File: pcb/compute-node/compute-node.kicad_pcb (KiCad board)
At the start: 2 copper layers, 30 x 26.8 mm, 6 parts, among them J1 UART, U1 PicoNode-Card, U2 STM32F030F4Px

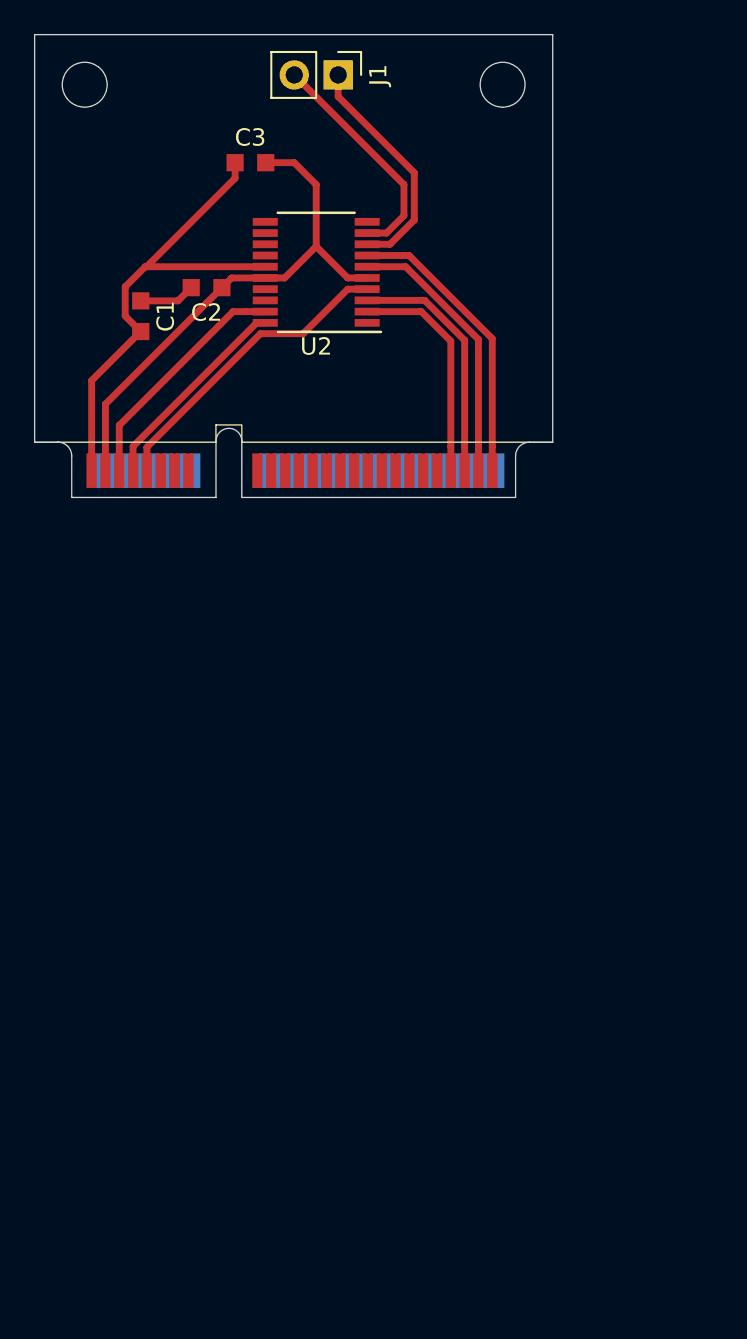
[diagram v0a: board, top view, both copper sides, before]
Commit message: Adopted compute node PCB to use pin headers
Since we currently don't have any 1mm PCB stock to use
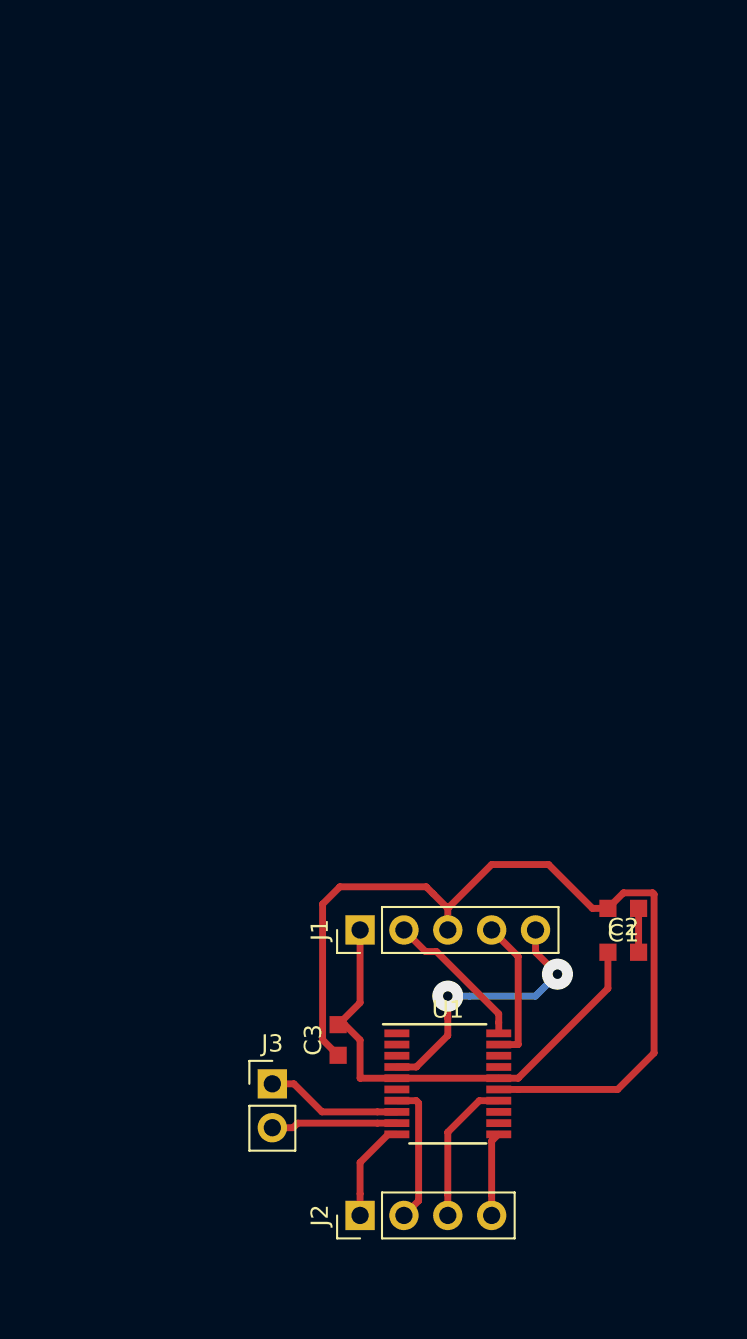
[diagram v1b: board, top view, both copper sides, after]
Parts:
- removed U2: STM32F030F4Px, Package_SO:TSSOP-20_4.4x6.5mm_P0.65mm
- added J2: PicoTalk, Connector_PinHeader_2.54mm:PinHeader_1x04_P2.54mm_Vertical, F.Cu at (134.6, 149.9)
- added J3: UART, Connector_PinHeader_2.54mm:PinHeader_1x02_P2.54mm_Vertical, F.Cu at (129.5, 142.2)
- J1: value UART -> STM32_SWD; footprint Connector_PinHeader_2.54mm:PinHeader_1x02_P2.54mm_Vertical -> Connector_PinHeader_2.54mm:PinHeader_1x05_P2.54mm_Vertical
- U1: value PicoNode-Card -> STM32F030F4Px; footprint mpcie:mpcie-half-card -> Package_SO:TSSOP-20_4.4x6.5mm_P0.65mm
- moved C3 51.1 mm to (133.3, 139.7), turned to 90 degrees
- moved J1 49.5 mm to (134.6, 133.3), turned to 90 degrees
- moved C2 45.4 mm to (149.9, 134.6), turned to 0 degrees
- moved C1 44.2 mm to (149.9, 132.1), turned to 180 degrees
- moved U1 35.1 mm to (139.7, 142.2)
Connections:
- J1 pad 1: Net-(J1-Pad1) -> VDD
- U1 pad 1: GND -> Net-(U1-Pad1)
- U1 pad 15: Net-(U1-Pad15) -> GND
- U1 pad 16: Net-(U1-Pad16) -> VDD
- U1 pad 19: Net-(U1-Pad19) -> Net-(J1-Pad4)
- U1 pad 20: Net-(U1-Pad20) -> Net-(J1-Pad2)
- U1 pad 3: VDD -> Net-(U1-Pad3)
- U1 pad 4: Net-(U1-Pad4) -> Net-(J1-Pad5)
- U1 pad 5: Net-(U1-Pad5) -> VDD
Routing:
- net GND: track 29.0 -> 52.1 mm
- net Net-(U1-Pad51): track 16.9 -> 0.00 mm
- net Net-(J1-Pad5): track 0.00 -> 15.9 mm, vias 0 -> 2
- net Net-(U1-Pad49): track 15.8 -> 0.00 mm
- net Net-(U1-Pad47): track 14.2 -> 0.00 mm
- net Net-(U1-Pad5): track 13.8 -> 0.00 mm
- net Net-(J1-Pad1): track 13.5 -> 0.00 mm
- net Net-(U1-Pad45): track 13.1 -> 0.00 mm
- net Net-(J3-Pad2): track 17.9 -> 7.32 mm
- net Net-(J2-Pad3): track 0.00 -> 8.53 mm
- net Net-(J1-Pad4): track 0.00 -> 8.40 mm
- net Net-(J3-Pad1): track 0.00 -> 7.88 mm
- net Net-(J2-Pad1): track 0.00 -> 5.87 mm
- net Net-(J2-Pad4): track 0.00 -> 4.88 mm
- net Net-(J1-Pad2): track 13.3 -> 8.63 mm
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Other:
- board outline removed

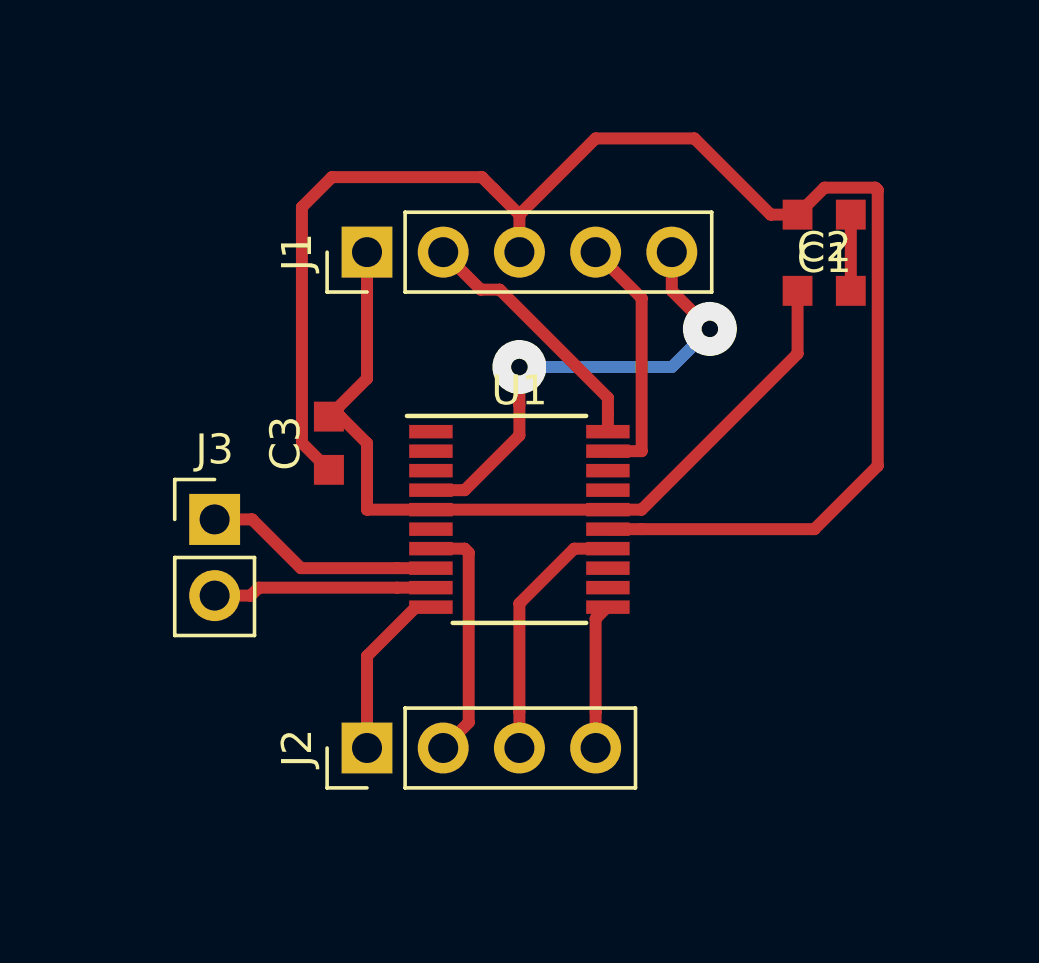
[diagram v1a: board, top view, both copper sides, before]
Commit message: Ground planes
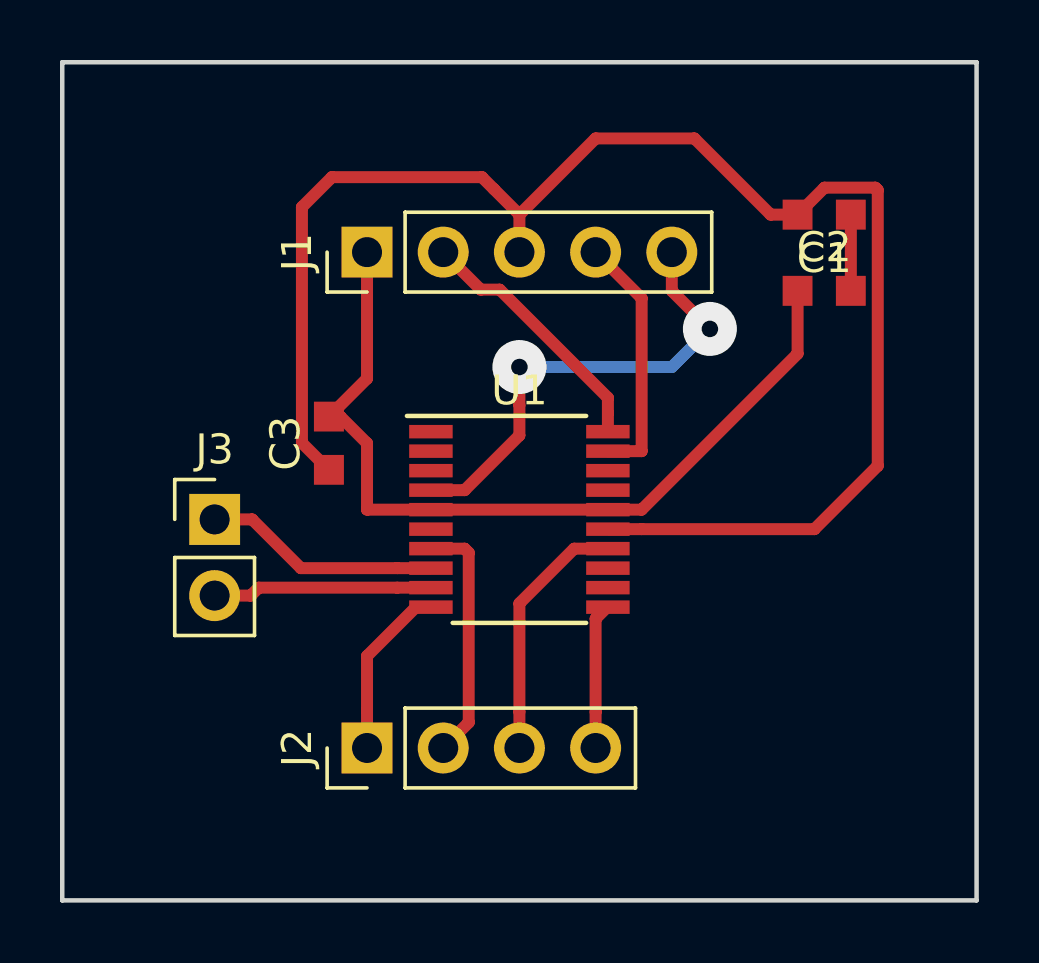
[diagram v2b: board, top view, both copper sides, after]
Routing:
- added copper zone on B.Cu, net GND
- added copper zone on F.Cu, net GND
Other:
- board outline added: 30.5 x 27.9 mm
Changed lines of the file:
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@@
   (general
     (thickness 1.6)
-    (drawings 0)
+    (drawings 4)
     (tracks 75)
     (zones 0)
@@
     )
   )
+  (gr_line (start 124.46 154.94) (end 124.46 127) (layer Edge.Cuts) (width 0.15))
+  (gr_line (start 154.94 154.94) (end 124.46 154.94) (layer Edge.Cuts) (width 0.15))
+  (gr_line (start 154.94 127) (end 154.94 154.94) (layer Edge.Cuts) (width 0.15))
+  (gr_line (start 124.46 127) (end 154.94 127) (layer Edge.Cuts) (width 0.15))
   (segment (start 134.62 137.545) (end 134.62 133.33) (width 0.4) (layer F.Cu) (net 2))
   (segment (start 133.3525 138.8125) (end 134.62 137.545) (width 0.4) (layer F.Cu) (net 2))
@@
   (segment (start 143.775001 134.865001) (end 143.775 139.965) (width 0.4) (layer F.Cu) (net 20))
   (segment (start 142.24 133.33) (end 143.775001 134.865001) (width 0.4) (layer F.Cu) (net 20))
+  (zone (net 4) (net_name GND) (layer F.Cu) (hatch edge 0.508)
+    (connect_pads (clearance 0.508))
+    (min_thickness 0.254)
+    (fill yes (arc_segments 16) (thermal_gap 0.508) (thermal_bridge_width 0.508))
+    (polygon
+      (pts
+        (xy 124.46 127) (xy 154.94 127) (xy 154.94 154.94) (xy 124.46 154.94)
+      )
+    )
+  )
+  (zone (net 4) (net_name GND) (layer B.Cu) (hatch edge 0.508)
+    (connect_pads (clearance 0.508))
+    (min_thickness 0.254)
+    (fill yes (arc_segments 16) (thermal_gap 0.508) (thermal_bridge_width 0.508))
+    (polygon
+      (pts
+        (xy 124.46 127) (xy 154.94 127) (xy 154.94 154.94) (xy 124.46 154.94)
+      )
+    )
+  )
 )

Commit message: Motherboard PCB
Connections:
- J3 pad 1: Net-(J3-Pad1) -> /TX
- J3 pad 2: Net-(J3-Pad2) -> /RX
- U1 pad 17: Net-(U1-Pad17) -> /TX
- U1 pad 18: Net-(U1-Pad18) -> /RX
- U1 pad 8: Net-(J3-Pad1) -> Net-(U1-Pad8)
- U1 pad 9: Net-(J3-Pad2) -> Net-(U1-Pad9)
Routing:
- net /RX: track 0.00 -> 29.3 mm, vias 0 -> 1
- net /TX: track 0.00 -> 23.3 mm, vias 0 -> 1
- net GND: track 52.1 -> 33.4 mm
- net Net-(J3-Pad1): track 7.88 -> 0.00 mm
- net Net-(J3-Pad2): track 7.32 -> 0.00 mm
- net VDD: track 28.5 -> 30.7 mm
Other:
- outline, holes or cut-outs redrawn
- board text added: "PicoNode Compute"
- board text added: "RX"
- board text added: "TX"

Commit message: Pin orientation
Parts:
- J1, J2: moved to B.Cu
- turned J1 to 270 degrees
- turned J2 to 270 degrees
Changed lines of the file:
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@@
-(kicad_pcb (version 20171130) (host pcbnew "(5.0.0-rc2-dev-616-g2f5fdcf32)")
+(kicad_pcb (version 20171130) (host pcbnew "(5.0.0-rc2-dev-620-g5d71153ea)")
   (general
     (thickness 1.6)
@@
     )
   )
-  (module Connector_PinHeader_2.54mm:PinHeader_1x04_P2.54mm_Vertical (layer F.Cu)
-    (at 134.62 149.86 90)
+  (module Connector_PinHeader_2.54mm:PinHeader_1x04_P2.54mm_Vertical (layer B.Cu)
+    (at 134.62 149.86 270)
     (descr "Through hole straight pin header, 1x04, 2.54mm pitch, single row")
     (tags "Through hole pin header THT 1x04 2.54mm single row")
-    (fp_text reference J2 (at 0 -2.33 90) (layer F.SilkS)
-      (effects (font (size 1 1) (thickness 0.15)))
-    )
-    (fp_text value PicoTalk (at 0 9.95 90) (layer F.Fab)
-      (effects (font (size 1 1) (thickness 0.15)))
-    )
-    (fp_line (start -0.635 -1.27) (end 1.27 -1.27) (layer F.Fab) (width 0.1))
-    (fp_line (start 1.27 -1.27) (end 1.27 8.89) (layer F.Fab) (width 0.1))
-    (fp_line (start 1.27 8.89) (end -1.27 8.89) (layer F.Fab) (width 0.1))
-    (fp_line (start -1.27 8.89) (end -1.27 -0.635) (layer F.Fab) (width 0.1))
-    (fp_line (start -1.27 -0.635) (end -0.635 -1.27) (layer F.Fab) (width 0.1))
-    (fp_line (start -1.33 8.95) (end 1.33 8.95) (layer F.SilkS) (width 0.12))
-    (fp_line (start -1.33 1.27) (end -1.33 8.95) (layer F.SilkS) (width 0.12))
-    (fp_line (start 1.33 1.27) (end 1.33 8.95) (layer F.SilkS) (width 0.12))
-    (fp_line (start -1.33 1.27) (end 1.33 1.27) (layer F.SilkS) (width 0.12))
-    (fp_line (start -1.33 0) (end -1.33 -1.33) (layer F.SilkS) (width 0.12))
-    (fp_line (start -1.33 -1.33) (end 0 -1.33) (layer F.SilkS) (width 0.12))
-    (fp_line (start -1.8 -1.8) (end -1.8 9.4) (layer F.CrtYd) (width 0.05))
-    (fp_line (start -1.8 9.4) (end 1.8 9.4) (layer F.CrtYd) (width 0.05))
-    (fp_line (start 1.8 9.4) (end 1.8 -1.8) (layer F.CrtYd) (width 0.05))
-    (fp_line (start 1.8 -1.8) (end -1.8 -1.8) (layer F.CrtYd) (width 0.05))
-    (fp_text user %R (at 0 3.81 180) (layer F.Fab)
-      (effects (font (size 1 1) (thickness 0.15)))
-    )
-    (pad 1 thru_hole rect (at 0 0 90) (size 1.7 1.7) (drill 1) (layers *.Cu *.Mask)
+    (fp_text reference J2 (at 0 2.33 270) (layer B.SilkS)
+      (effects (font (size 1 1) (thickness 0.15)) (justify mirror))
+    )
+    (fp_text value PicoTalk (at 0 -9.95 270) (layer B.Fab)
+      (effects (font (size 1 1) (thickness 0.15)) (justify mirror))
+    )
+    (fp_line (start -0.635 1.27) (end 1.27 1.27) (layer B.Fab) (width 0.1))
+    (fp_line (start 1.27 1.27) (end 1.27 -8.89) (layer B.Fab) (width 0.1))
+    (fp_line (start 1.27 -8.89) (end -1.27 -8.89) (layer B.Fab) (width 0.1))
+    (fp_line (start -1.27 -8.89) (end -1.27 0.635) (layer B.Fab) (width 0.1))
+    (fp_line (start -1.27 0.635) (end -0.635 1.27) (layer B.Fab) (width 0.1))
+    (fp_line (start -1.33 -8.95) (end 1.33 -8.95) (layer B.SilkS) (width 0.12))
+    (fp_line (start -1.33 -1.27) (end -1.33 -8.95) (layer B.SilkS) (width 0.12))
+    (fp_line (start 1.33 -1.27) (end 1.33 -8.95) (layer B.SilkS) (width 0.12))
+    (fp_line (start -1.33 -1.27) (end 1.33 -1.27) (layer B.SilkS) (width 0.12))
+    (fp_line (start -1.33 0) (end -1.33 1.33) (layer B.SilkS) (width 0.12))
+    (fp_line (start -1.33 1.33) (end 0 1.33) (layer B.SilkS) (width 0.12))
+    (fp_line (start -1.8 1.8) (end -1.8 -9.4) (layer B.CrtYd) (width 0.05))
+    (fp_line (start -1.8 -9.4) (end 1.8 -9.4) (layer B.CrtYd) (width 0.05))
+    (fp_line (start 1.8 -9.4) (end 1.8 1.8) (layer B.CrtYd) (width 0.05))
+    (fp_line (start 1.8 1.8) (end -1.8 1.8) (layer B.CrtYd) (width 0.05))
+    (fp_text user %R (at 0 -3.81 180) (layer B.Fab)
+      (effects (font (size 1 1) (thickness 0.15)) (justify mirror))
+    )
+    (pad 1 thru_hole rect (at 0 0 270) (size 1.7 1.7) (drill 1) (layers *.Cu *.Mask)
       (net 14 "Net-(J2-Pad1)"))
-    (pad 2 thru_hole oval (at 0 2.54 90) (size 1.7 1.7) (drill 1) (layers *.Cu *.Mask)
+    (pad 2 thru_hole oval (at 0 -2.54 270) (size 1.7 1.7) (drill 1) (layers *.Cu *.Mask)
       (net 15 "Net-(J2-Pad2)"))
-    (pad 3 thru_hole oval (at 0 5.08 90) (size 1.7 1.7) (drill 1) (layers *.Cu *.Mask)
+    (pad 3 thru_hole oval (at 0 -5.08 270) (size 1.7 1.7) (drill 1) (layers *.Cu *.Mask)
       (net 12 "Net-(J2-Pad3)"))
-    (pad 4 thru_hole oval (at 0 7.62 90) (size 1.7 1.7) (drill 1) (layers *.Cu *.Mask)
+    (pad 4 thru_hole oval (at 0 -7.62 270) (size 1.7 1.7) (drill 1) (layers *.Cu *.Mask)
       (net 11 "Net-(J2-Pad4)"))
     (model ${KISYS3DMOD}/Connector_PinHeader_2.54mm.3dshapes/PinHeader_1x04_P2.54mm_Vertical.wrl
@@
     )
   )
-  (module Connector_PinHeader_2.54mm:PinHeader_1x05_P2.54mm_Vertical (layer F.Cu)
-    (at 134.62 133.33 90)
+  (module Connector_PinHeader_2.54mm:PinHeader_1x05_P2.54mm_Vertical (layer B.Cu)
+    (at 134.62 133.33 270)
     (descr "Through hole straight pin header, 1x05, 2.54mm pitch, single row")
     (tags "Through hole pin header THT 1x05 2.54mm single row")
-    (fp_text reference J1 (at 0 -2.33 90) (layer F.SilkS)
-      (effects (font (size 1 1) (thickness 0.15)))
-    )
-    (fp_text value STM32_SWD (at 0 12.49 90) (layer F.Fab)
-      (effects (font (size 1 1) (thickness 0.15)))
-    )
-    (fp_line (start -0.635 -1.27) (end 1.27 -1.27) (layer F.Fab) (width 0.1))
-    (fp_line (start 1.27 -1.27) (end 1.27 11.43) (layer F.Fab) (width 0.1))
-    (fp_line (start 1.27 11.43) (end -1.27 11.43) (layer F.Fab) (width 0.1))
-    (fp_line (start -1.27 11.43) (end -1.27 -0.635) (layer F.Fab) (width 0.1))
-    (fp_line (start -1.27 -0.635) (end -0.635 -1.27) (layer F.Fab) (width 0.1))
-    (fp_line (start -1.33 11.49) (end 1.33 11.49) (layer F.SilkS) (width 0.12))
-    (fp_line (start -1.33 1.27) (end -1.33 11.49) (layer F.SilkS) (width 0.12))
-    (fp_line (start 1.33 1.27) (end 1.33 11.49) (layer F.SilkS) (width 0.12))
-    (fp_line (start -1.33 1.27) (end 1.33 1.27) (layer F.SilkS) (width 0.12))
-    (fp_line (start -1.33 0) (end -1.33 -1.33) (layer F.SilkS) (width 0.12))
-    (fp_line (start -1.33 -1.33) (end 0 -1.33) (layer F.SilkS) (width 0.12))
-    (fp_line (start -1.8 -1.8) (end -1.8 11.95) (layer F.CrtYd) (width 0.05))
-    (fp_line (start -1.8 11.95) (end 1.8 11.95) (layer F.CrtYd) (width 0.05))
-    (fp_line (start 1.8 11.95) (end 1.8 -1.8) (layer F.CrtYd) (width 0.05))
-    (fp_line (start 1.8 -1.8) (end -1.8 -1.8) (layer F.CrtYd) (width 0.05))
-    (fp_text user %R (at 0 5.08 180) (layer F.Fab)
-      (effects (font (size 1 1) (thickness 0.15)))
-    )
-    (pad 1 thru_hole rect (at 0 0 90) (size 1.7 1.7) (drill 1) (layers *.Cu *.Mask)
+    (fp_text reference J1 (at 0 2.33 270) (layer B.SilkS)
+      (effects (font (size 1 1) (thickness 0.15)) (justify mirror))
+    )
+    (fp_text value STM32_SWD (at 0 -12.49 270) (layer B.Fab)
+      (effects (font (size 1 1) (thickness 0.15)) (justify mirror))
+    )
+    (fp_line (start -0.635 1.27) (end 1.27 1.27) (layer B.Fab) (width 0.1))
+    (fp_line (start 1.27 1.27) (end 1.27 -11.43) (layer B.Fab) (width 0.1))
+    (fp_line (start 1.27 -11.43) (end -1.27 -11.43) (layer B.Fab) (width 0.1))
+    (fp_line (start -1.27 -11.43) (end -1.27 0.635) (layer B.Fab) (width 0.1))
+    (fp_line (start -1.27 0.635) (end -0.635 1.27) (layer B.Fab) (width 0.1))
+    (fp_line (start -1.33 -11.49) (end 1.33 -11.49) (layer B.SilkS) (width 0.12))
+    (fp_line (start -1.33 -1.27) (end -1.33 -11.49) (layer B.SilkS) (width 0.12))
+    (fp_line (start 1.33 -1.27) (end 1.33 -11.49) (layer B.SilkS) (width 0.12))
+    (fp_line (start -1.33 -1.27) (end 1.33 -1.27) (layer B.SilkS) (width 0.12))
+    (fp_line (start -1.33 0) (end -1.33 1.33) (layer B.SilkS) (width 0.12))
+    (fp_line (start -1.33 1.33) (end 0 1.33) (layer B.SilkS) (width 0.12))
+    (fp_line (start -1.8 1.8) (end -1.8 -11.95) (layer B.CrtYd) (width 0.05))
+    (fp_line (start -1.8 -11.95) (end 1.8 -11.95) (layer B.CrtYd) (width 0.05))
+    (fp_line (start 1.8 -11.95) (end 1.8 1.8) (layer B.CrtYd) (width 0.05))
+    (fp_line (start 1.8 1.8) (end -1.8 1.8) (layer B.CrtYd) (width 0.05))
+    (fp_text user %R (at 0 -5.08 180) (layer B.Fab)
+      (effects (font (size 1 1) (thickness 0.15)) (justify mirror))
+    )
+    (pad 1 thru_hole rect (at 0 0 270) (size 1.7 1.7) (drill 1) (layers *.Cu *.Mask)
       (net 2 VDD))
-    (pad 2 thru_hole oval (at 0 2.54 90) (size 1.7 1.7) (drill 1) (layers *.Cu *.Mask)
+    (pad 2 thru_hole oval (at 0 -2.54 270) (size 1.7 1.7) (drill 1) (layers *.Cu *.Mask)
       (net 8 "Net-(J1-Pad2)"))
-    (pad 3 thru_hole oval (at 0 5.08 90) (size 1.7 1.7) (drill 1) (layers *.Cu *.Mask)
+    (pad 3 thru_hole oval (at 0 -5.08 270) (size 1.7 1.7) (drill 1) (layers *.Cu *.Mask)
       (net 4 GND))
-    (pad 4 thru_hole oval (at 0 7.62 90) (size 1.7 1.7) (drill 1) (layers *.Cu *.Mask)
+    (pad 4 thru_hole oval (at 0 -7.62 270) (size 1.7 1.7) (drill 1) (layers *.Cu *.Mask)
       (net 16 "Net-(J1-Pad4)"))
-    (pad 5 thru_hole oval (at 0 10.16 90) (size 1.7 1.7) (drill 1) (layers *.Cu *.Mask)
+    (pad 5 thru_hole oval (at 0 -10.16 270) (size 1.7 1.7) (drill 1) (layers *.Cu *.Mask)
       (net 13 "Net-(J1-Pad5)"))
     (model ${KISYS3DMOD}/Connector_PinHeader_2.54mm.3dshapes/PinHeader_1x05_P2.54mm_Vertical.wrl
